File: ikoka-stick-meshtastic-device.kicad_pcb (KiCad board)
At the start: 2 copper layers, 100 x 28 mm, 26 parts, among them J1 Conn_Coaxial, J2 Conn_01x07_Socket, J3 Conn_01x07_Socket, J4 Conn_01x02, J5 Conn_01x02, J6 Conn_01x04, Q1 AO3401A, SW1 SW_Push, U1 MT3608, U2 E22-900M30S, U3 XIAO-ESP32-S3-SMD

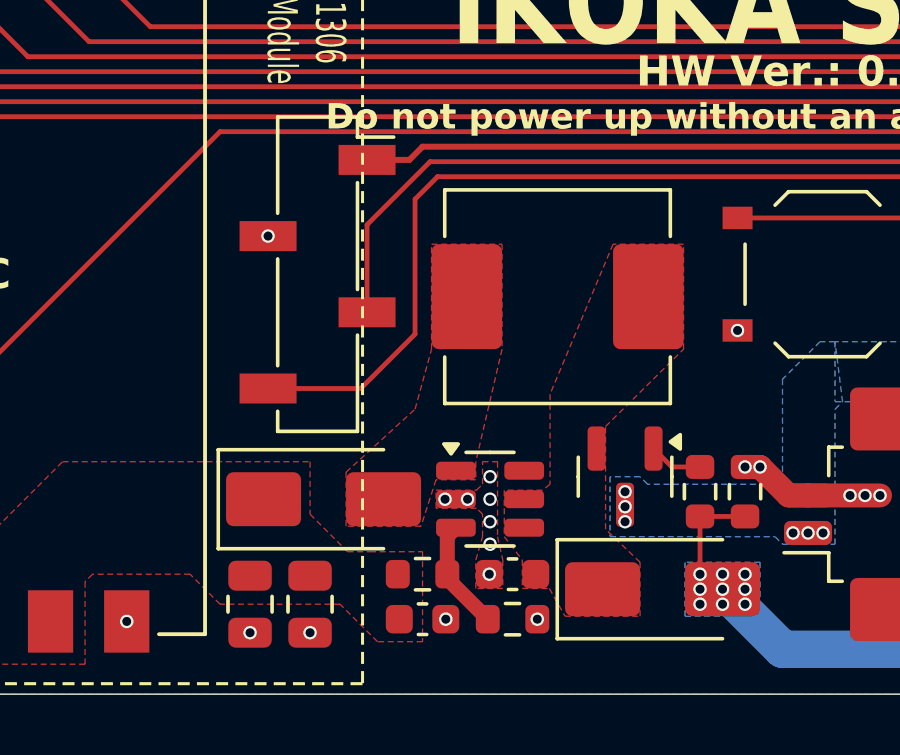
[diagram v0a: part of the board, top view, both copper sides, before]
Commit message: fix: Route PS1, sync PCB nets from schematic and clean up DRC
- Update J3.5, J6.3, J6.4 pad nets to match schematic (+3V3, /I2C_SCL, /I2C_SDA)
- Rotate PS1 header 180 deg in place so BOOST_IN lands in its pour; route
  PS1.4 to the +5V2_LORA pour with a 0.6 mm F.Cu track
- Remove leftover no-net zone and orphan GND vias from the old booster; refill zones
- Include PS1 in BOM to match the symbol
- Use ${KIPRJMOD} for the Booster_Module footprint library path
- PCB and project saved in KiCad 10 format

DRC: 0 errors, 0 unconnected, 0 parity issues.

Co-Authored-By: Claude Opus 5.5 <noreply@anthropic.com>
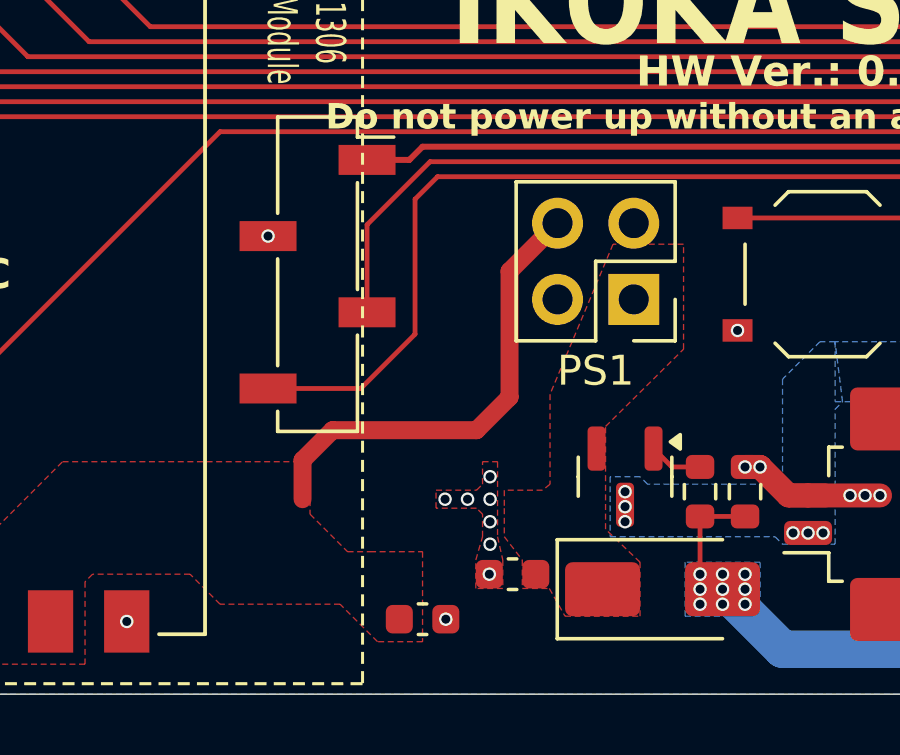
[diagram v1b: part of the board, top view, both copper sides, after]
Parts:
- removed C3, C4: 47uF, Capacitor_SMD:C_0805_2012Metric
- removed D1: SS34, Diode_SMD:D_SMA
- removed L1: 22uH, Inductor_SMD:L_Sunlord_MWSA0624S
- removed R1: 300K, Resistor_SMD:R_0603_1608Metric
- removed R2: 39K, Resistor_SMD:R_0603_1608Metric
- removed U1: MT3608, Package_TO_SOT_SMD:SOT-23-6
- added PS1: XL3608 5V Boost (wired), Connector_PinHeader_2.54mm:PinHeader_2x02_P2.54mm_Vertical, F.Cu at (183.5, 100.8)
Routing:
- net +5V2_LORA: track 0.00 -> 15.5 mm
- net Net-(U1-FB): track 3.73 -> 0.00 mm
- net GND: vias 142 -> 139
- removed copper zone on F.Cu, net Net-(D1-A)

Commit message: feat: v2 - drop 21700 battery, mount XL3608 module on the back
- Remove BT1 (21700 holder) and its B.Cu +BATT pours/vias; trim the F.Cu
  +BATT strip to J5. Board is powered from the XIAO USB 5V.
- Keep D3 (VBUS backfeed block), C1, and the Q1/R3/R4 power path with
  J4/J5 for an optional LiPo; rejoin Q1-J4-J5 with a back track.
- New footprint Booster_XL3608_24.4x13.7mm_SMD (SMD pads only, assumed
  positions, VIN/VOUT/GND silk labels). PS1 placed on B.Cu, vertical, under
  the old header spot, clear of the E22 RF area. Only its own pads are
  exposed under the module (vias tented).
- Silkscreen HW Ver. 2.0.0; README power section updated.

DRC: 0 errors, 0 unconnected, 0 parity issues.

Co-Authored-By: Claude Opus 5.5 <noreply@anthropic.com>
Claude-Session: https://claude.ai/code/session_013aihWTyEvMfq2tmgNbS7qs
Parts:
- removed BT1: Battery_Cell, Battery 21700:BatteryHolder_MYOUNG_BH-21700-B1BJ001_1x21700
- PS1: value XL3608 5V Boost (wired) -> XL3608 5V Boost module (back); footprint Connector_PinHeader_2.54mm:PinHeader_2x02_P2.54mm_Vertical -> Booster_Module:Booster_XL3608_24.4x13.7mm_SMD; moved to B.Cu
- moved PS1 5.11 mm to (178.5, 100.0), turned to 90 degrees
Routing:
- net +BATT: track 0.00 -> 18.4 mm, vias 9 -> 3
- net /BOOST_IN: track 0.00 -> 11.3 mm, vias 0 -> 1
- net +5V2_LORA: track 15.5 -> 12.4 mm, vias 0 -> 1
- removed copper zone on B.Cu, net +BATT
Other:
- board text added: "HW Ver.: 2.0.0"
- board text removed: "HW Ver.: 0.3.0"
